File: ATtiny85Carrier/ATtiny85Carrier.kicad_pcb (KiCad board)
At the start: 2 copper layers, 17 parts, among them J2 Header, J3 GND Header, SW1 Power_SW, U1 ATtiny85-20PU, U2 L78L05_TO92

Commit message: Finalized and exported board
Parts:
- added G***: LOGO, libraries:attiny85Image, B.Cu at (127.0, 125.7)
- moved SW1 67.8 mm to (116.3, 147.1), turned to 270 degrees
- moved R7 42.8 mm to (137.7, 126.5), turned to 270 degrees
- moved D2 42.7 mm to (130.6, 148.8), turned to 180 degrees
- moved R3 30.5 mm to (121.8, 112.8), turned to 270 degrees
- moved R6 25.2 mm to (118.5, 112.8), turned to 270 degrees
- moved R1 23.9 mm to (135.0, 112.8), turned to 270 degrees
- moved J2 21.7 mm to (120.4, 106.7), turned to 90 degrees
- moved J3 17.6 mm to (120.4, 102.6), turned to 90 degrees
- moved D1 15.9 mm to (120.9, 126.5), turned to 270 degrees
- moved R2 13.2 mm to (128.4, 112.8), turned to 270 degrees
- moved BT1 12.5 mm to (116.3, 135.6)
- moved R4 12.5 mm to (131.7, 112.8), turned to 270 degrees
- moved R5 8.52 mm to (125.1, 112.8), turned to 270 degrees
- moved U1 2.30 mm to (125.5, 129.0)
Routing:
- net Net-(C1-Pad1): track 0.00 -> 26.6 mm
- net +5V: track 0.00 -> 26.3 mm
- net Net-(D2-Pad1): track 0.00 -> 18.2 mm
- net Net-(R1-Pad2): track 0.00 -> 15.2 mm
- net Net-(BT1-Pad1): track 0.00 -> 13.7 mm
- net Net-(R4-Pad2): track 0.00 -> 13.1 mm
- net Net-(R3-Pad2): track 0.00 -> 12.7 mm
- net Net-(R2-Pad2): track 0.00 -> 11.5 mm
- net Net-(R6-Pad2): track 0.00 -> 10.7 mm
- net Net-(R5-Pad2): track 0.00 -> 10.3 mm
- net +9V: track 0.00 -> 9.77 mm
- net Net-(J2-Pad6): track 0.00 -> 6.89 mm
- net Net-(J2-Pad1): track 0.00 -> 6.89 mm
- net Net-(J2-Pad2): track 0.00 -> 6.57 mm
- net Net-(J2-Pad5): track 0.00 -> 6.57 mm
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- added copper zone on B.Cu, net GND
- added copper zone on F.Cu, net GND
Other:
- board outline added: 27.3 x 55.2 mm
- board text added: "+"
- board text added: "-"
- board text added: "9V"
- board text added: "ATtiny85 Carrier V1.0"
- board text added: "GND"
- board text added: "JLCJLCJLCJLC"
- board text added: "PB0"
- board text added: "PB1"
- board text added: "PB2"
- board text added: "PB3"
- board text added: "PB4"
- board text added: "PB5"
- board text added: "Thomas McDonagh"

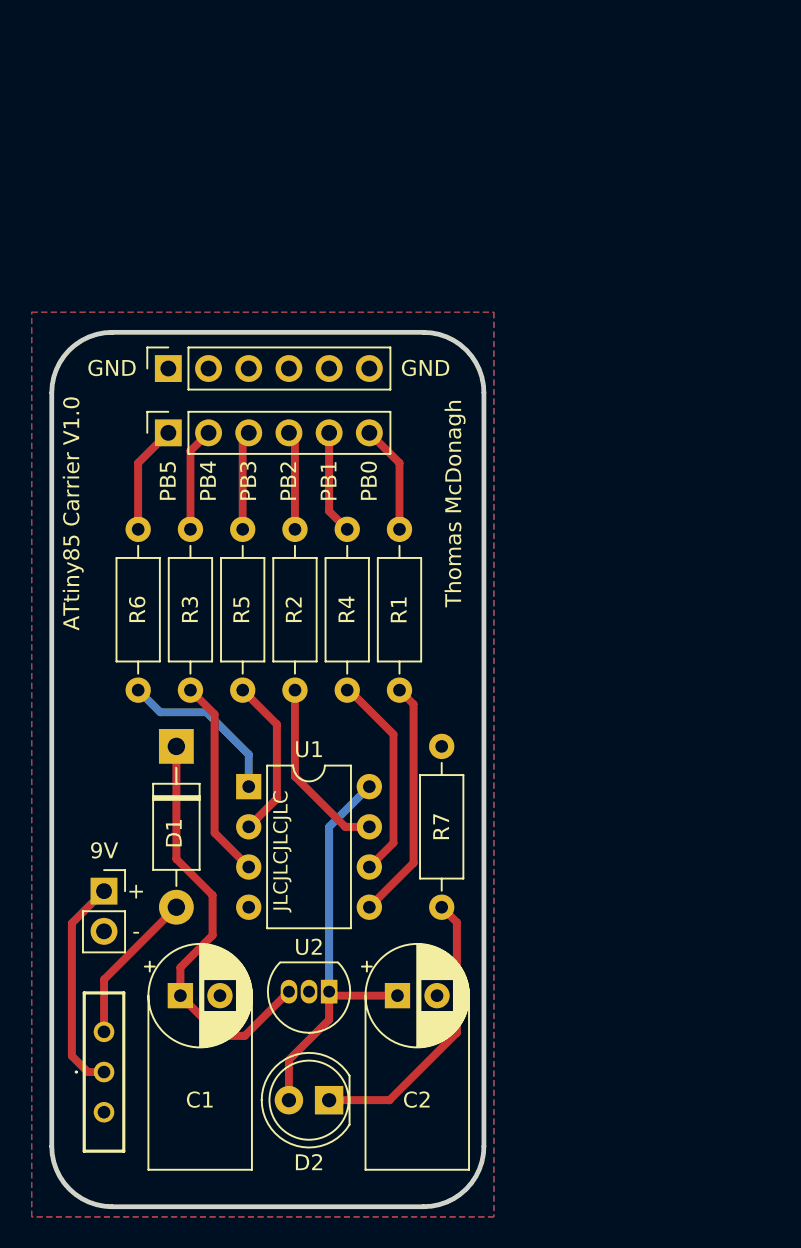
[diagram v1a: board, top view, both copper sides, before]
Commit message: Added mounting holes and replotted gerbers
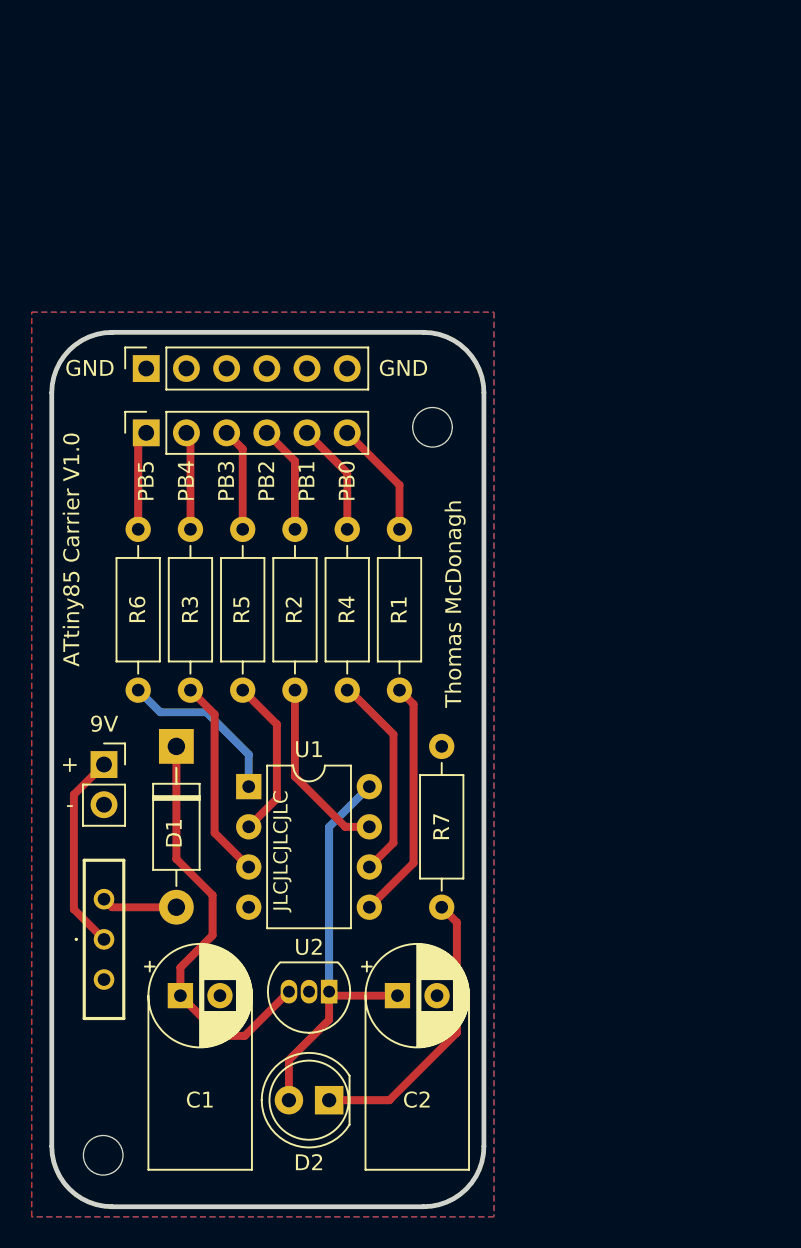
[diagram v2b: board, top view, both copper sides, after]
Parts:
- added H1: MountingHole, MountingHole:MountingHole_2.5mm, F.Cu at (116.3, 152.3)
- added H2: MountingHole, MountingHole:MountingHole_2.5mm, F.Cu at (137.1, 106.3)
- moved G*** 12.3 mm to (127.1, 138.0)
- moved SW1 8.38 mm to (116.3, 138.7)
- moved BT1 8.00 mm to (116.3, 127.6)
- moved J2 1.40 mm to (119.0, 106.7)
- moved J3 1.40 mm to (119.0, 102.6)
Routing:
- net +9V: track 9.77 -> 4.78 mm
- net Net-(BT1-Pad1): track 13.7 -> 12.6 mm
- net Net-(J2-Pad5): track 6.57 -> 7.15 mm
- net Net-(J2-Pad1): track 6.89 -> 6.31 mm
- net Net-(J2-Pad4): track 6.25 -> 6.83 mm
- net Net-(J2-Pad6): track 6.89 -> 7.46 mm
